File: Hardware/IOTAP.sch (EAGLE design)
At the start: 48 parts, among them IC1 MCP9808-MSOP8, J1 POWER_JACK-SLOTS, J2 PoE, SW1 MODE

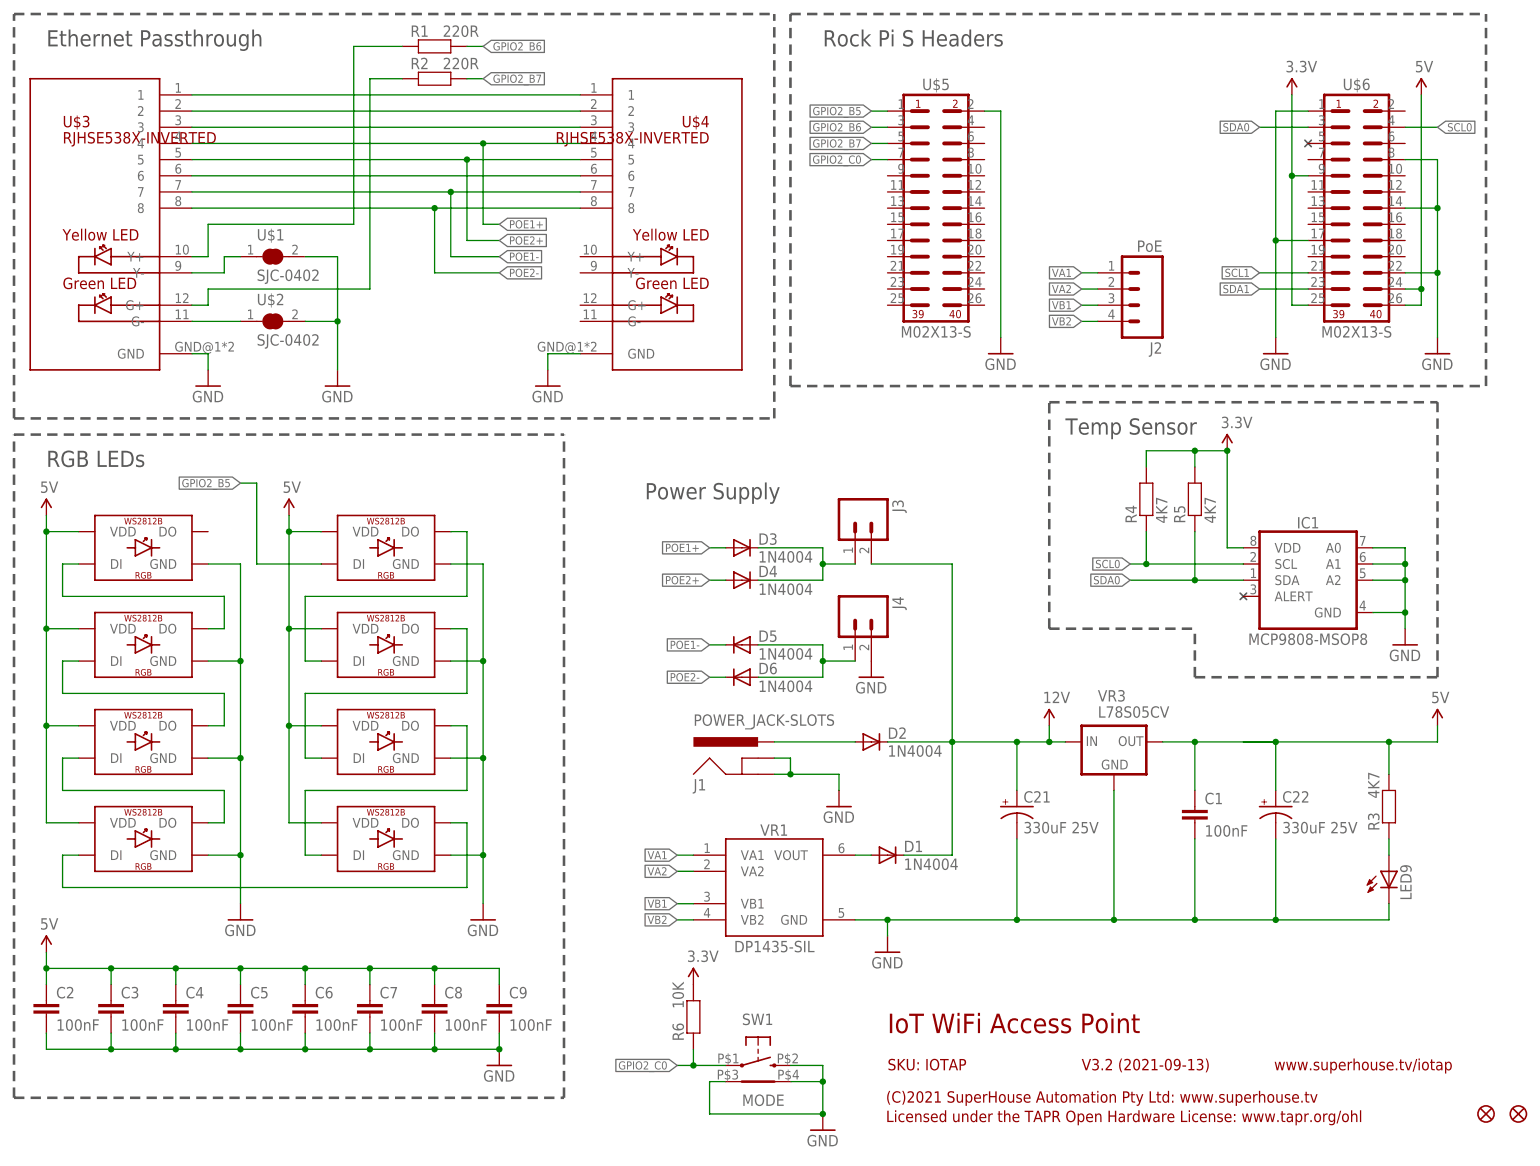
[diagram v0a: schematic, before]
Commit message: Fixed footprint for RJ45 socket.
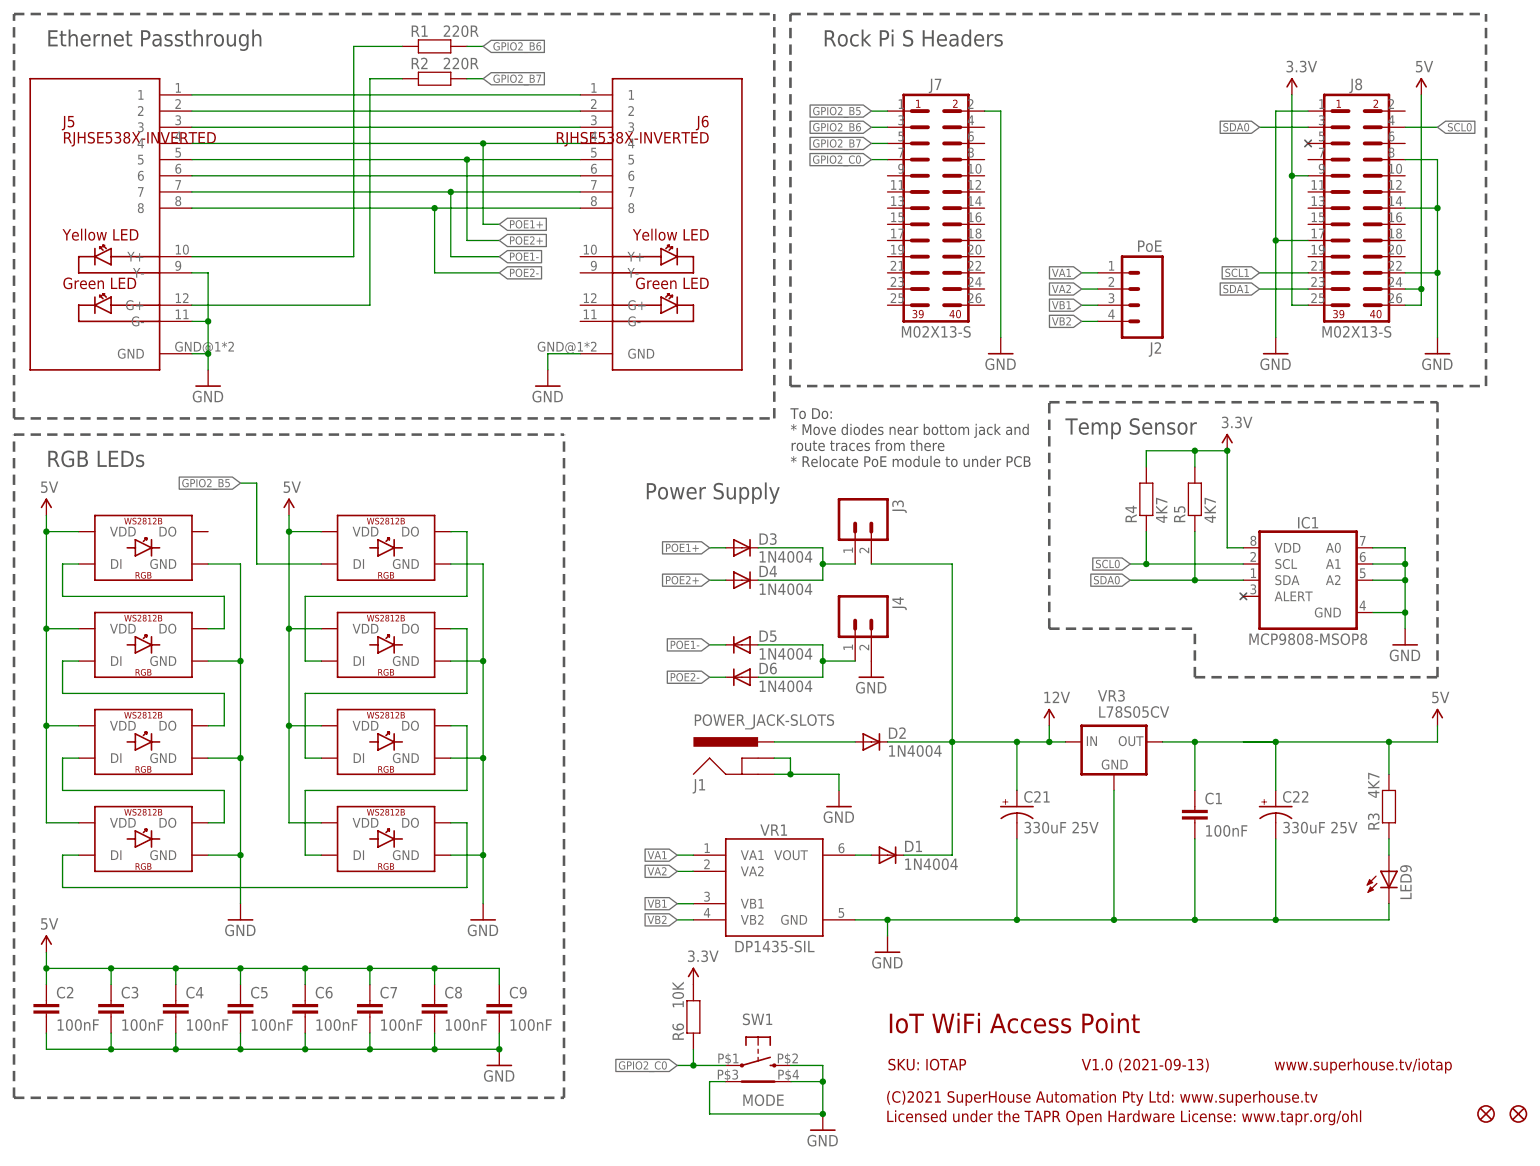
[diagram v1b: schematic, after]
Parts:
- removed U$1, U$2: SJC-0402, SuperHouse-Jumpers:SJC-0402
- renumbered U$3 to J5, U$4 to J6, U$5 to J7, U$6 to J8
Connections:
- removed net N$21: J5.Y-, U$1.1
- removed net N$24: J5.G-, U$2.1
- net GND: now also J5.G-, J5.Y-; no longer U$1.2, U$2.2
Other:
- note added: "To Do: * Move diodes near bottom jack and route traces from there * Relocate PoE module to under PCB"
- note added: "V1.0 (2021-09-13)"
- note removed: "V3.2 (2021-09-13)"

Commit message: Major redesign based on Raspberry Pi Zero 2.
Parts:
- removed D5, D6: 1N4004, SuperHouse-Diodes:DIODESMA
- removed IC1: MCP9808-MSOP8, SuperHouse-Sensors:MCP9808-MSOP8
- removed J7, J8: M02X13-S, SuperHouse-Connectors:M02X13-S
- added C10, C14, C18: 10nF, SuperHouse-Capacitors:CAP0603
- added C11: 330uF 50V, SuperHouse-Capacitors:CAP_POLG
- added C12, C13: 18pF, SuperHouse-Capacitors:CAP0603
- added C15: 22nF, SuperHouse-Capacitors:CAP0603
- added C16: 4.7uF, SuperHouse-Capacitors:CAP0603
- added C17, C20: 10uF, SuperHouse-Capacitors:CAP0805
- added C19, C23, C24, C25: 100nF, SuperHouse-Capacitors:CAP0603
- added FID3: FIDUCIAL1X2.5, SuperHouse-Symbols:FIDUCIAL1X2.5
- added IC2: CAT24C32-SOIC8, SuperHouse-ICs:CAT24C32-SOIC8
- added IC3: CAT24C32-UDFN8, SuperHouse-ICs:CAT24C32-UDFN8
- added IC4: W5500-LQFP, SuperHouse-ICs:W5500-LQFP
- added IC5: MCP24AA025E48-SOT23-6, SuperHouse-ICs:MCP24AA025E48-SOT23-6
- added IC6: AT30TSE752A-SOIC8, SuperHouse-Sensors:AT30TSE752A-SOIC8
- added L1: SMDRI127-330MT, SuperHouse-Inductors:INDUCTORCDRH127
- added L2: 1uH 250mA 0805, rcl:L-USL2012C
- added LED10, LED11, LED12: GREEN, SuperHouse-LEDs:LED0603
- added LED13: YELLOW, SuperHouse-LEDs:LED0603
- added MOD1: RASPI-ZERO-INV, SuperHouse-Modules:RASPI-ZERO-INV
- added Q1: 2N7002, SuperHouse-Transistors:MOSFET-NCHANNEL-233
- added R10, R11, R8, R9: 49R9 1%, SuperHouse-Resistors:RESISTOR0603
- added R12, R13, R14, R15, R16, R17: 470R, SuperHouse-Resistors:RESISTOR0603
- added R18, R22, R23: 10K, SuperHouse-Resistors:RESISTOR0603
- added R19, R20: 4K7, SuperHouse-Resistors:RESISTOR0603
- added R21: 1K, SuperHouse-Resistors:RESISTOR0603
- added R26: 12.4K 1%, SuperHouse-Resistors:RESISTOR0603
- added R31: 1M, SuperHouse-Resistors:RESISTOR0603
- added R7: 10R, SuperHouse-Resistors:RESISTOR0603
- added RN1, RN2: 10K, SuperHouse-Resistors:4R-NCAY16
- added SJ1: CE0, SuperHouse-Jumpers:SJC-NORMAL
- added SJ2: CE2, SuperHouse-Jumpers:SJ-NORMAL
- added VR2: LM2596S-5.0, SuperHouse-Regulators:LM2596S-XX
- added XTL1: 25MHz, SuperHouse-Oscillators:CRYSTAL-GND3X2
- C21: value 330uF 25V -> 330uF 50V
- D1, D2, D3: value 1N4004 -> SS56
- D4: value 1N4004 -> PMEG3050EP,115; device SuperHouse-Diodes:DIODESMA -> SuperHouse-Diodes:DIODE-SOD128
- J2: value PoE -> !WRITE; device SuperHouse-Connectors:M04-SOCKET -> SuperHouse-Connectors:M02-PLAIN
- J5: value RJHSE538X-INVERTED -> ARJM11D7-114-AB-EW2; device SuperHouse-Connectors:RJHSE538X-INVERTED -> SuperHouse-Connectors:ARJM11D7-114-AB-EW2
- J6: value RJHSE538X-INVERTED -> (none); device SuperHouse-Connectors:RJHSE538X-INVERTED -> SuperHouse-Connectors:QWIICJS-1MM
- LED9: value (none) -> BLUE
- R1, R2: value 220R -> 10K
- VR1: value DP1435-SIL -> DP1435-12V
- VR3: value L78S05CV -> AP2112KSOT25; device SuperHouse-Regulators:78XX-L78XX-FLAT -> SuperHouse-Regulators:AP2112KSOT25
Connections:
- removed net GPIO2_B5: J7.1, LED1.DI
- removed net GPIO2_B6: J7.3, R1.2
- removed net GPIO2_B7: J7.5, R2.2
- removed net GPIO2_C0: J7.7, R6.1, SW1.1
- removed net N$6: J5.Y+, R1.1
- removed net N$7: D5.A, D6.A, J4.1
- removed net N$8: J5.G+, R2.1
- removed net POE1+: D3.A, J5.4, J6.4
- removed net POE1-: D5.C, J5.7, J6.7
- removed net POE2+: D4.A, J5.5, J6.5
- removed net POE2-: D6.C, J5.8, J6.8
- removed net SCL0: IC1.SCL, J8.4, R4.1
- removed net SCL1: J8.21
- removed net SDA0: IC1.SDA, J8.3, R5.1
- removed net SDA1: J8.23
- new net !ETH_CS: IC4.!CS, SJ1.2, SJ2.2
- new net 1V2O: C14.1, IC4.1V2O
- new net 3V3A: C18.1, C20.1, C23.1, C24.1, C25.1, IC4.3V3A, L2.2
- new net ACTLED: IC4.!ACT, R12.2, R14.1
- new net FDXLED: IC4.!DPX, R15.1
- new net ID_SCL: IC2.SCL, IC3.SCL, MOD1.IO1, R20.1
- new net ID_SDA: IC2.SDA, IC3.SDA, MOD1.IO0, R19.1
- new net IO10_COPI: MOD1.IO10_COPI
- new net IO11_SCK: MOD1.IO11_SCLK
- new net IO12_LEDS: MOD1.IO12, Q1.S, R2.1
- new net IO16_!CE2: MOD1.IO16, SJ2.1
- new net IO17_!ETH_RST: IC4.!RESET, MOD1.IO17, R1.1
- new net IO18_!CE0: MOD1.IO18, SJ1.1
- new net IO19_CIPO1: IC4.CIPO, MOD1.IO19_CIPO1
- new net IO20_COPI1: IC4.COPI, MOD1.IO20_COPI1
- new net IO21_SCK1: IC4.SCLK, MOD1.IO21_SCLK1
- new net IO25_!ETH_INT: IC4.!INT, MOD1.IO25, R22.1
- new net IO2_SDA: IC5.SDA, IC6.SDA, J6.3, MOD1.IO2_SDA, R5.1
- new net IO3_SCL: IC5.SCL, IC6.SCL, J6.4, MOD1.IO3_SCL, R4.1
- new net IO6_!BUTTON: MOD1.IO6, R6.1, SW1.1
- new net IO8: MOD1.IO8
- new net IO9_CIPO: MOD1.IO9_CIPO
- new net LEDS: LED1.DI, Q1.D, R18.1
- new net LINKLED: IC4.!LINK, R13.2, R17.1
- new net N$18: C13.1, IC4.XO, R31.1, XTL1.2
- new net N$20: C10.1, J5.RCT, R10.1, R11.1
- new net N$26: LED12.C, R16.2
- new net N$27: C12.1, IC4.XI/CLKIN, R31.2, XTL1.1
- new net N$28: LED13.C, R17.2
- new net N$31: C16.1, IC4.TOCAP
- new net N$32: C15.1, J5.TCT, R7.2
- new net N$327: LED11.C, R15.2
- new net N$329: LED10.C, R14.2
- new net N$33: IC4.EXRES1, R26.1
- new net N$34: IC4.RSVD, R23.1
- new net N$36: IC4.MOD0, RN1A.1
- new net N$37: IC4.MOD1, RN1B.1
- new net N$38: IC4.MOD2, RN1C.1
- new net N$39: IC4.RSVD5, RN1D.1
- new net N$40: IC4.RSVD4, RN2A.1
- new net N$41: IC4.RSVD3, RN2B.1
- new net N$42: IC4.RSVD2, RN2C.1
- new net N$43: IC4.RSVD1, RN2D.1
- new net RXIN: IC4.RXIN, J5.RD-, R11.2
- new net RXIP: IC4.RXIP, J5.RD+, R10.2
- new net SPDLED: IC4.!SPD, R16.1
- new net TXON: IC4.TXON, J5.TD-, R9.1
- new net TXOP: IC4.TXOP, J5.TD+, R8.1
- net 12V: now also C11.+, D3.C, VR2.VIN; no longer J3.2, VR3.IN
- net 3.3V: now also C17.1, C19.1, IC2.VCC, IC3.VCC, IC4.3V3D, IC5.VCC, IC6.VCC, J5.GRN_A, J5.YEL_A, J6.2, L2.1, LED10.A, LED11.A, LED12.A, LED13.A, Q1.G, R1.2, R19.2, R2.2, R20.2, R21.2, R22.2, R3.2, R7.1, R8.2, R9.2, RN1A.2, RN1B.2, RN1C.2, VR3.VOUT; no longer IC1.VDD, J8.25, J8.9
- net 5V: now also L1.2, MOD1.5V, R18.2, VR2.FB, VR3.EN, VR3.VIN; no longer J8.24, J8.26, R3.2, VR3.OUT
- net GND: now also C10.2, C11.-, C12.2, C13.2, C14.2, C15.2, C16.2, C17.2, C18.2, C19.2, C20.2, C23.2, C24.2, C25.2, D4.A, IC2.A0, IC2.A1, IC2.A2, IC2.GND, IC3.A0, IC3.A1, IC3.A2, IC3.GND, IC4.AGND, IC4.GND, IC5.A0, IC5.A1, IC5.GND, IC6.A0, IC6.A1, IC6.A2, IC6.GND, J2.2, J6.1, MOD1.GND, R23.2, R26.2, RN1D.2, RN2A.2, RN2B.2, RN2C.2, RN2D.2, VR2.!EN, VR2.GND, XTL1.GND; no longer IC1.A0, IC1.A1, IC1.A2, IC1.GND, J5.G-, J5.Y-, J6.GND, J7.2, J8.1, J8.14, J8.17, J8.22, J8.8
- net N$1: now also D3.A, J3.2; no longer J5.1, J6.1
- net N$2: now also D4.C, L1.1, VR2.VOUT; no longer J5.2, J6.2
- net N$3: now also J5.YEL_K, R13.1; no longer J5.3, J6.3
- net N$4: now also J5.GRN_K, R12.1; no longer J5.6, J6.6
- net N$5: now also IC2.WP, IC3.WP, J2.1, R21.1; no longer D3.C, D4.C, J3.1
- net VA1: now also J5.VC1+; no longer J2.1
- net VA2: now also J5.VC1-; no longer J2.2
- net VB1: now also J3.1, J5.VC2+; no longer J2.3
- net VB2: now also J4.1, J5.VC2-; no longer J2.4
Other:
- note added: "(C)2022 SuperHouse Automation Pty Ltd: www.superhouse.tv"
- note added: "3.3V Regulator"
- note added: "3.3VA Decoupling"
- note added: "5V Regulator"
- note added: "Ethernet CS Selector"
- note added: "Ethernet Interface with PoE"
- note added: "Ethernet Status"
- note added: "ID EEPROM"
- note added: "MAC Address ROM"
- note added: "Mod0-2 pulled high enables all modes. Strong external pullups improves EMC performance."
- note added: "Mode Button"
- note added: "NOTE: Dual footprint. Place either IC2 or IC3, but not both."
- note added: "Power Source Options"
- note added: "Raspberry Pi Zero 2 Headers"
- note added: "This power sourcing arrangement is naive, but could it work with the addition of an isolation relay on the raw input when powered by the DP1435, in place of the jumpers? If the supply voltage is too low to run the DP1435, it won't do anything and things are fine. If it is high enough, its output will turn on and fire the relay, isolating the direct inputs. This leaves a short delay when the LM258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"
- note added: "To Do: * Auto-switch PoE destination?"
- note added: "V2.0 (2022-06-16)"
- note added: "Wiznet W5500 !INT is an open-collector output. The 10K pull-up allows Ethernet activity to be detected when this signal is pulled LOW."
- note added: "Wiznet W5500 Ethernet Controller"
- note removed: "(C)2021 SuperHouse Automation Pty Ltd: www.superhouse.tv"
- note removed: "Ethernet Passthrough"
- note removed: "Power Supply"
- note removed: "Rock Pi S Headers"
- note removed: "To Do: * Move diodes near bottom jack and route traces from there * Relocate PoE module to under PCB"
- note removed: "V1.0 (2021-09-13)"
